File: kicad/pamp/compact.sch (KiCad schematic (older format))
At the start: 99 parts, among them J1 input, J3 output, J4 power, Q10 BC546B, Q11 MJE340, Q12 2SA1381F, Q13 2SC3503F, Q14 BC546B, Q15 BC556B, Q3 2SA1381F, Q6 BC560C, Q8 BC560C, Q9 BC556B

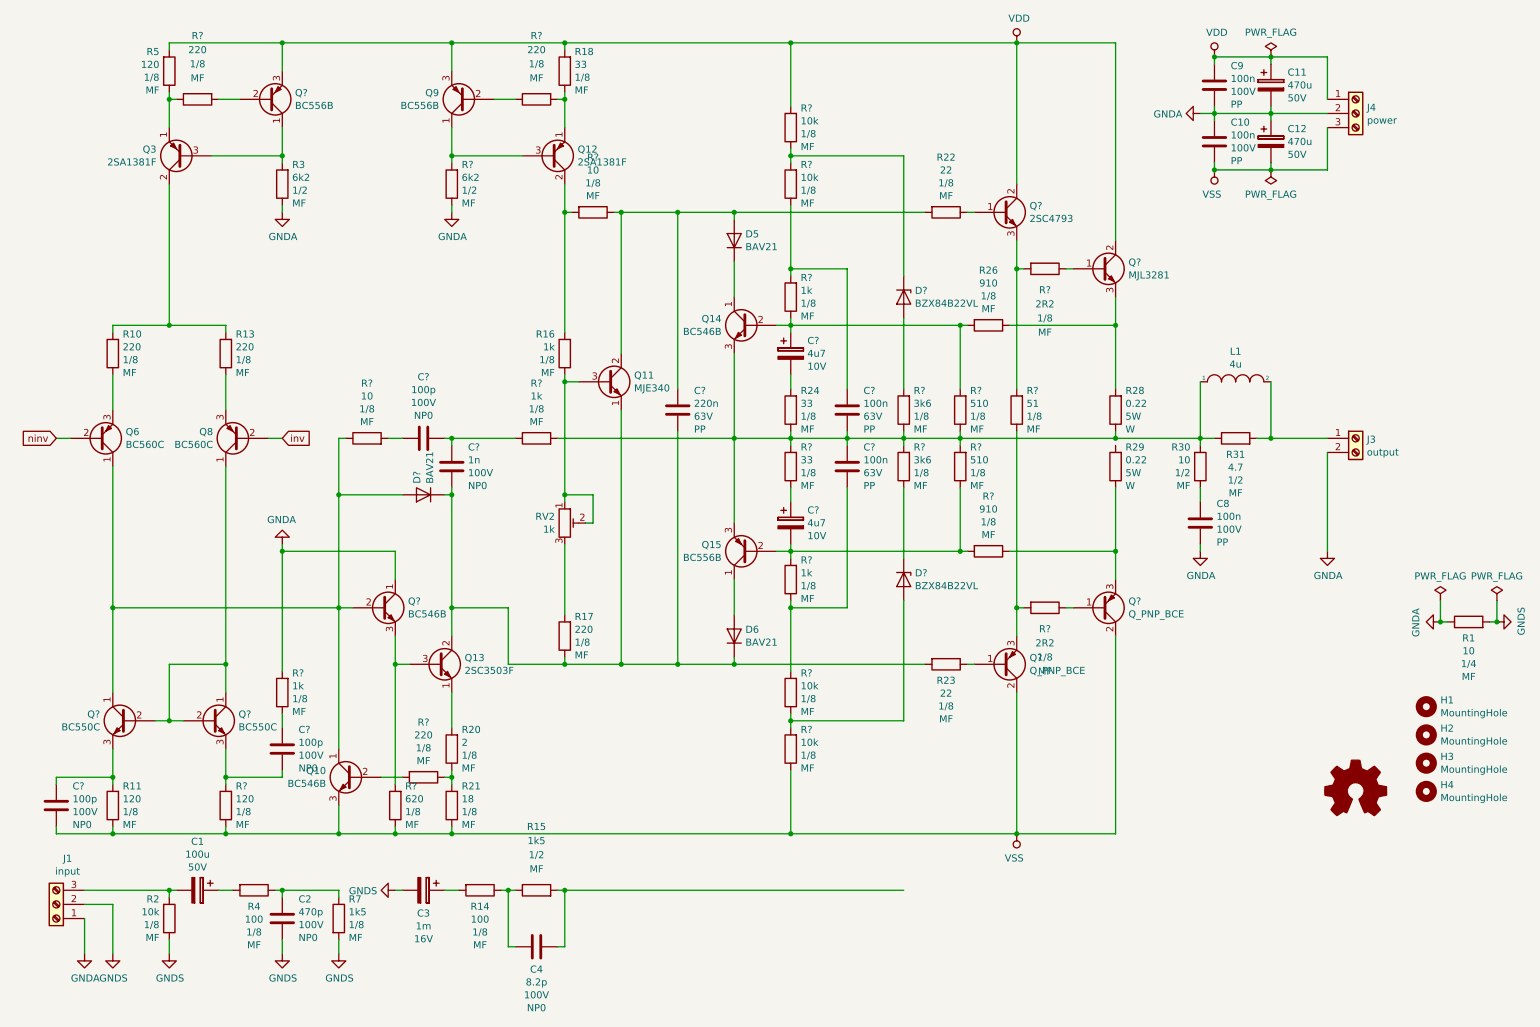
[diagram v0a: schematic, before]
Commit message: Schematic was made more simple.
Signed-off-by: Nenad Radulovic <nenad.b.radulovic@gmail.com>
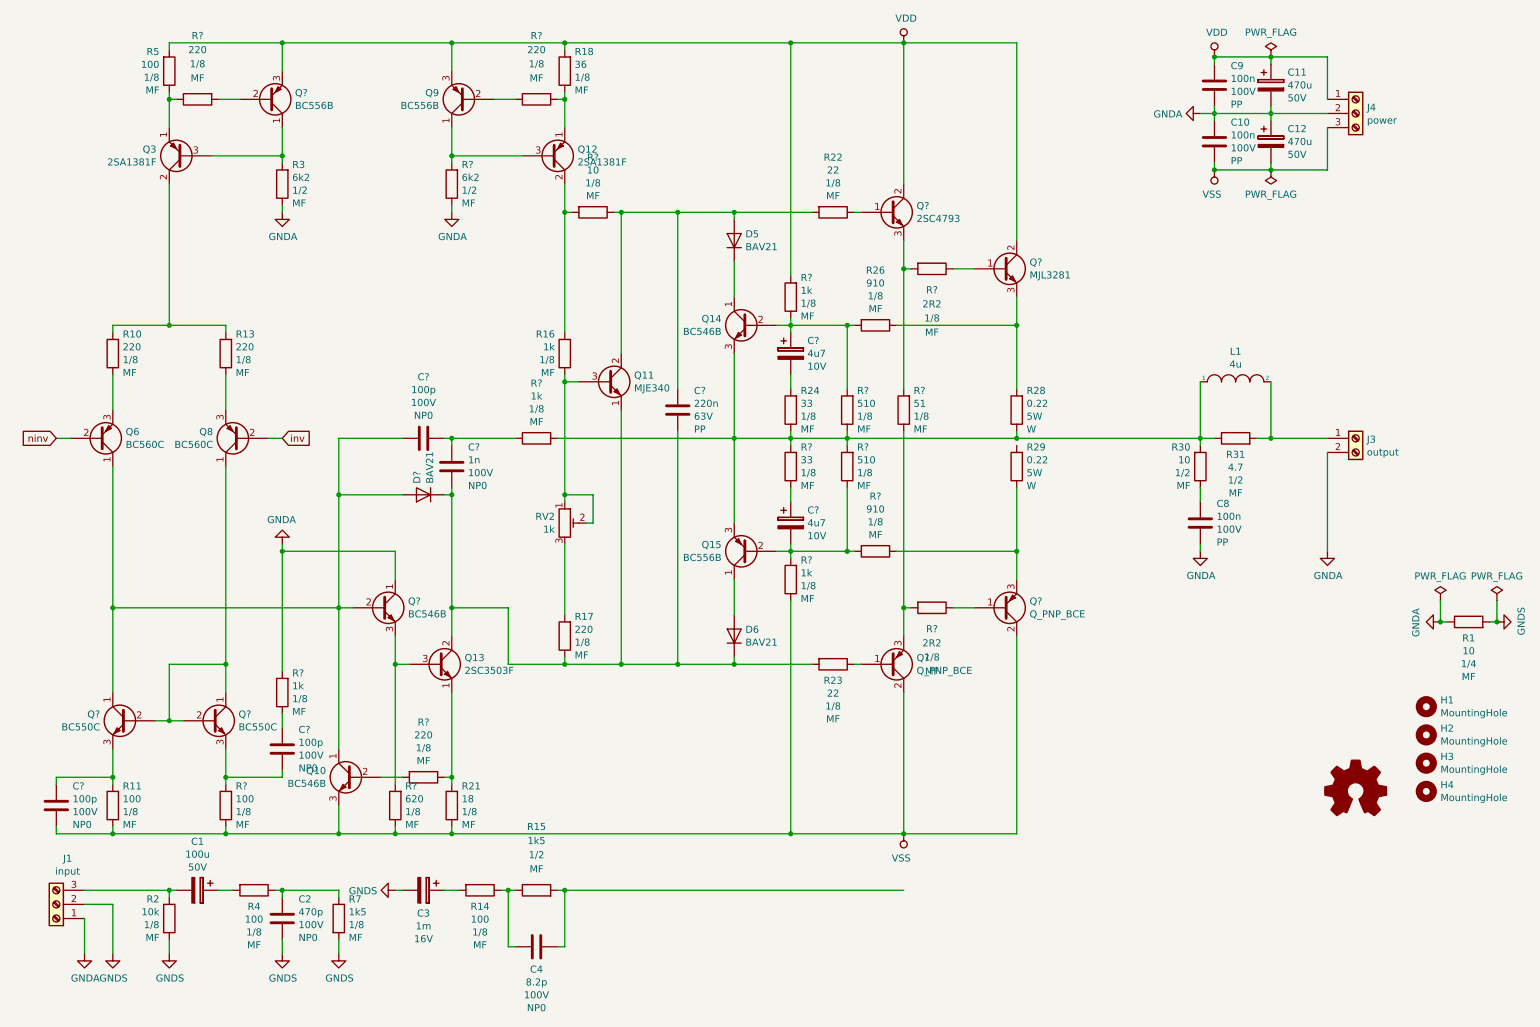
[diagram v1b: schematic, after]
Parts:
- removed C? (x2): 100n, Capacitor_THT:C_Rect_L7.2mm_W2.5mm_P5.00mm_FKS2_FKP2_MKS2_MKP2, symbol Device:C
- removed D? (x2): BZX84B22VL, Diode_THT:D_DO-41_SOD81_P7.62mm_Horizontal, symbol Device:D_Zener
- removed R20: 2, Resistor_THT:R_Axial_DIN0207_L6.3mm_D2.5mm_P10.16mm_Horizontal, symbol Device:R
- removed R? (x4): 10k, Resistor_THT:R_Axial_DIN0207_L6.3mm_D2.5mm_P10.16mm_Horizontal, symbol Device:R
- removed R? (x2): 3k6, Resistor_THT:R_Axial_DIN0207_L6.3mm_D2.5mm_P10.16mm_Horizontal, symbol Device:R
- removed R?: 10, Resistor_THT:R_Axial_DIN0207_L6.3mm_D2.5mm_P10.16mm_Horizontal, symbol Device:R
- R11, R5, R?: value 120 -> 100
- R18: value 33 -> 36
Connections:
- net VDD: now also R?.2
- net VSS: now also R?.1
- net at Q13.1 (E): now also R21.2, R?.1
- net at D?.2 (A), Q10.1 (C), Q6.1 (C)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: now also C?.2
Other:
- moved on the sheet: Q?, R22, R23, R26, R28, R29, R?

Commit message: Tweaked OPS protection curve.
Signed-off-by: Nenad Radulovic <nenad.b.radulovic@gmail.com>
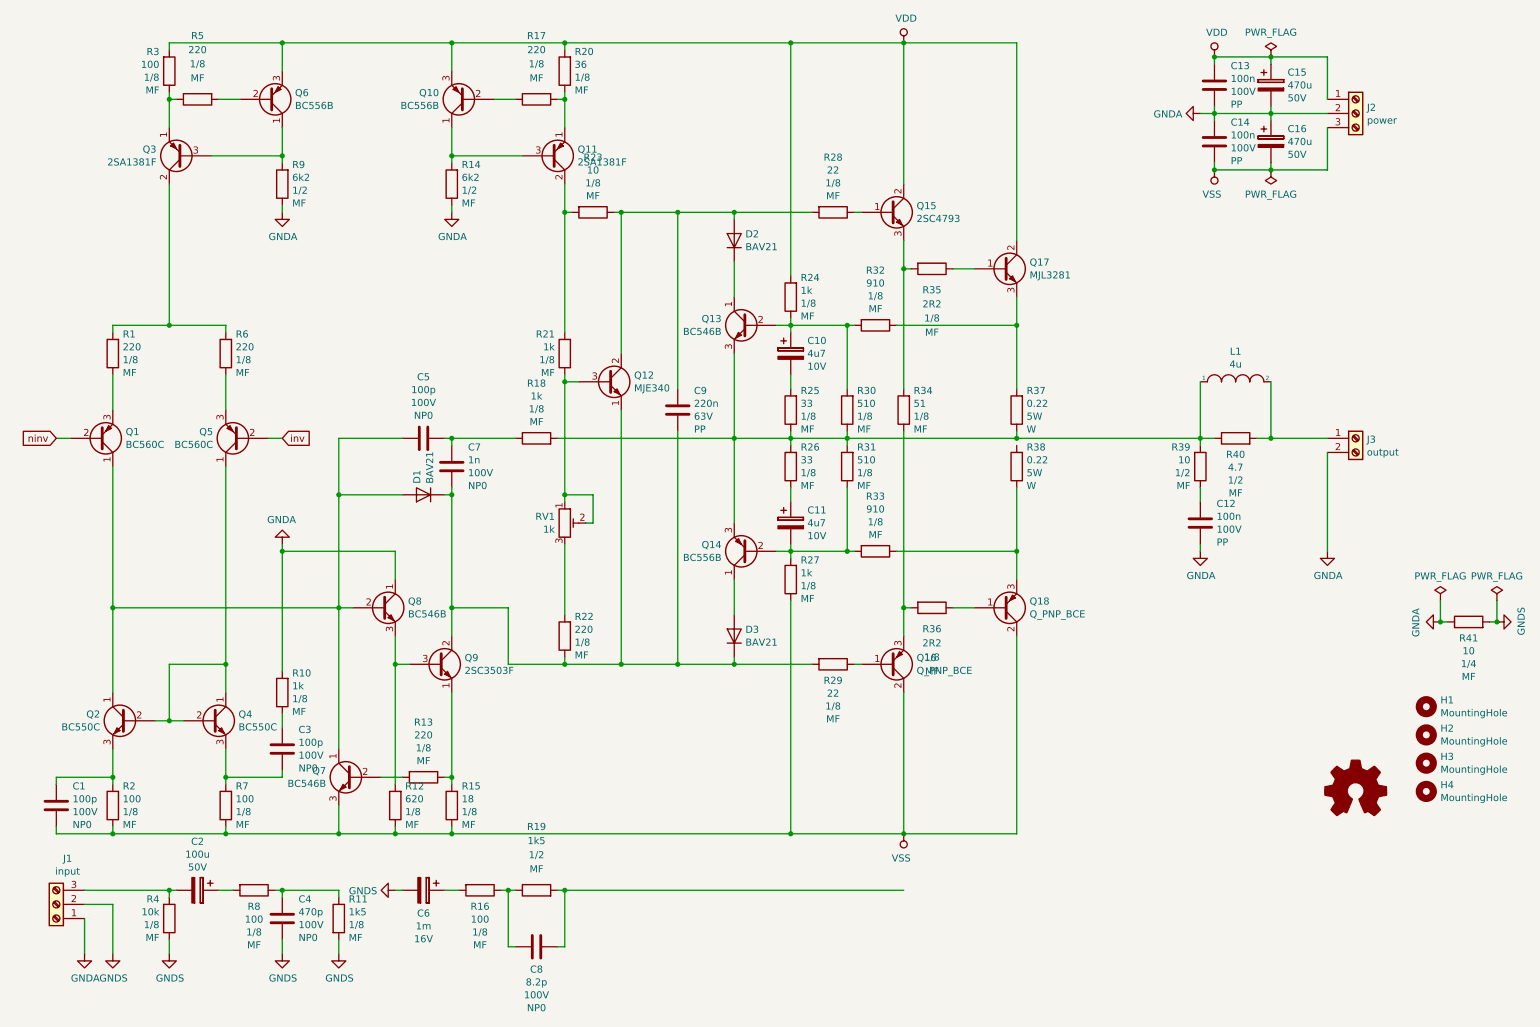
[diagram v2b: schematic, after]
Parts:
- gave numbers to parts that had none: 34
- renumbered C8 to C12, C9 to C13, C10 to C14, C11 to C15, C12 to C16, C1 to C2, C2 to C4, C3 to C6, C4 to C8, D5 to D2, D6 to D3, J4 to J2, Q6 to Q1, Q9 to Q10, Q12 to Q11, Q11 to Q12, Q14 to Q13, Q15 to Q14, Q8 to Q5, Q10 to Q7, Q13 to Q9, R10 to R1, R7 to R11, R21 to R15, R14 to R16, R15 to R19, R11 to R2, R18 to R20, R16 to R21, R17 to R22, R24 to R25, R22 to R28, R23 to R29, R5 to R3, R26 to R32, R28 to R37, R29 to R38, R30 to R39, R2 to R4, R31 to R40, R1 to R41, R13 to R6, R4 to R8, R3 to R9, RV2 to RV1

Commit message: Finished SPICE simulation, Kicad follows the updates
The VAS standing current was increased from 12mA to 15mA to avoid
VAS lower transistor switch-off during slewing. The VBE multiplier
was optimized for lower current-to-voltage dependency by increasing
collector resistor to 43 ohm. Also, the VBE resistor divider was
chosen in such way that we get around 8.9mV/C characteristic.

Kicad schematic was updated according to changes in Spice schematic.

Signed-off-by: Nenad Radulovic <nenad.b.radulovic@gmail.com>
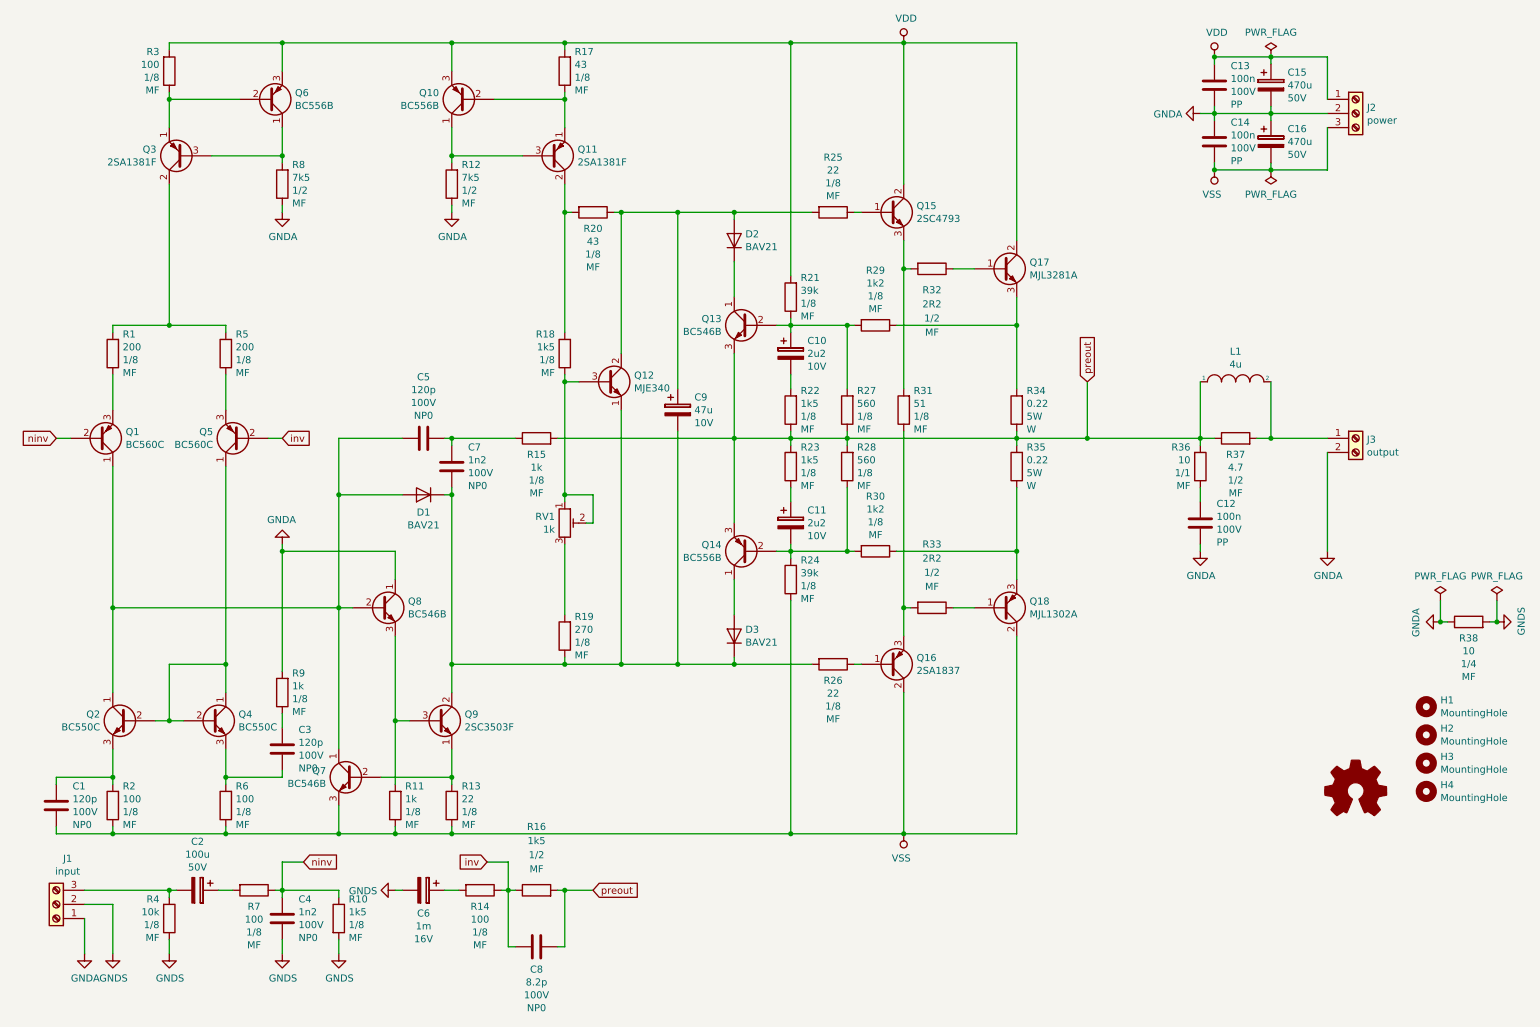
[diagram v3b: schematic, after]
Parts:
- removed C9: 220n, Capacitor_THT:C_Rect_L7.2mm_W4.5mm_P5.00mm_FKS2_FKP2_MKS2_MKP2, symbol Device:C
- removed R13, R17, R5: 220, Resistor_THT:R_Axial_DIN0207_L6.3mm_D2.5mm_P10.16mm_Horizontal, symbol Device:R
- removed R36: 2R2, Resistor_THT:R_Axial_DIN0207_L6.3mm_D2.5mm_P10.16mm_Horizontal, symbol Device:R
- added C9: 47u, Capacitor_THT:CP_Radial_D6.3mm_P2.50mm, symbol Device:CP
- added R33: 2R2, Resistor_THT:R_Axial_DIN0411_L9.9mm_D3.6mm_P12.70mm_Horizontal, symbol Device:R
- C1, C3, C5: value 100p -> 120p
- C10, C11: value 4u7 -> 2u2
- C4: value 470p -> 1n2; footprint Capacitor_THT:C_Disc_D3.8mm_W2.6mm_P2.50mm -> Capacitor_THT:C_Disc_D8.0mm_W2.5mm_P5.00mm
- C7: value 1n -> 1n2
- Q16: value Q_PNP_BCE -> 2SA1837; footprint (none) -> Package_TO_SOT_THT:TO-220-3_Vertical
- Q17: value MJL3281 -> MJL3281A; footprint Package_TO_SOT_THT:TO-220-3_Vertical -> Package_TO_SOT_THT:TO-264-3_Vertical
- Q18: value Q_PNP_BCE -> MJL1302A; footprint (none) -> Package_TO_SOT_THT:TO-264-3_Vertical
- R1: value 220 -> 200
- R11: renamed from R12; value 620 -> 1k
- R12: renamed from R14; value 6k2 -> 7k5
- R13: renamed from R15; value 18 -> 22
- R17: renamed from R20; value 36 -> 43
- R18: renamed from R21; value 1k -> 1k5
- R19: renamed from R22; value 220 -> 270
- R20: renamed from R23; value 10 -> 43
- R21: renamed from R24; value 1k -> 39k
- R22: renamed from R25; value 33 -> 1k5
- R23: renamed from R26; value 33 -> 1k5
- R24: renamed from R27; value 1k -> 39k
- R27: renamed from R30; value 510 -> 560
- R28: renamed from R31; value 510 -> 560
- R29: renamed from R32; value 910 -> 1k2
- R30: renamed from R33; value 910 -> 1k2
- R32: renamed from R35; footprint Resistor_THT:R_Axial_DIN0207_L6.3mm_D2.5mm_P10.16mm_Horizontal -> Resistor_THT:R_Axial_DIN0411_L9.9mm_D3.6mm_P12.70mm_Horizontal; Power 1/8 -> 1/2
- R36: renamed from R39; footprint Resistor_THT:R_Axial_DIN0411_L9.9mm_D3.6mm_P12.70mm_Horizontal -> Resistor_THT:R_Axial_DIN0414_L11.9mm_D4.5mm_P5.08mm_Vertical; Power 1/2 -> 1/1
- R5: renamed from R6; value 220 -> 200
- R8: renamed from R9; value 6k2 -> 7k5
- renumbered R11 to R10, R16 to R14, R18 to R15, R19 to R16, R28 to R25, R29 to R26, R34 to R31, R37 to R34, R38 to R35, R40 to R37, R41 to R38, R7 to R6, R8 to R7, R10 to R9
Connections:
- net inv: now also C8.2, R14.1, R16.1
- net ninv: now also C4.2, R10.1, R7.1
- net at D2.2 (A), Q12.2 (C), R20.1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: now also C9.1
- net preout: now reaches L1.1, Q13.3 (E), Q14.3 (E), R15.2, R22.1, R23.2, R27.1, R28.2, R34.1, R36.2, R37.1
- net preout: now also C8.1, R16.2, R35.2
- net at C7.1, D1.1 (K), D3.1 (K)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: now also C9.2
- net at Q9.1 (E), R13.2: now also Q7.2 (B)
- net at Q10.2 (B): now also Q11.1 (E), R17.1
- net at Q16.3 (E), R31.1: now also R33.2
- net at Q6.2 (B): now also Q3.1 (E), R3.1
- net at Q18.1 (B): now also R33.1
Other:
- moved on the sheet: Q9
